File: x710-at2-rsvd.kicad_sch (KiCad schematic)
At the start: 37 parts, among them J8 PinHeader_1x3_P2.54mm_Drill1.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, U9 EZX710AT2_S_LMR5

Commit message: [#86351] Rename project
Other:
- title: 10GbE Expansion -> OCuLink to 10GbE adapter

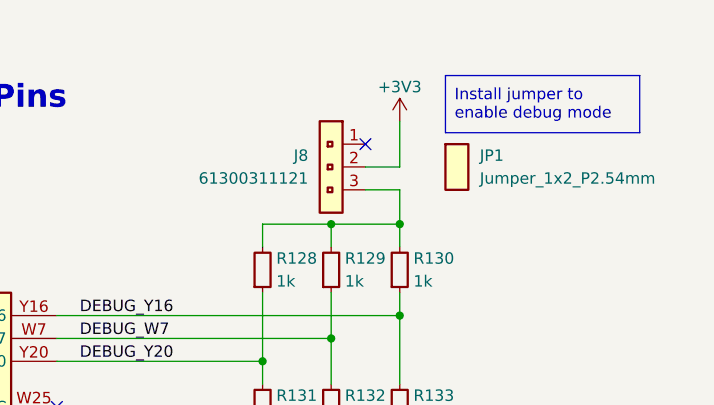
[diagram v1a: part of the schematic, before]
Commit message: [#86617] Change debug EN jumper to a switch
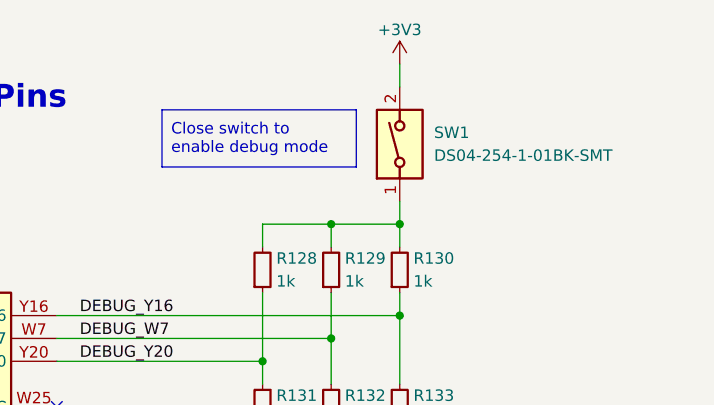
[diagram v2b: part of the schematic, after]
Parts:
- removed J8: PinHeader_1x3_P2.54mm_Drill1.1mm, antmicro-footprints:PinHeader_1x3_P2.54mm_Drill1.1mm, symbol antmicroGenericPinHeaders:PinHeader_1x3_P2.54mm_Drill1.1mm
- removed JP1: Jumper_1x2_P2.54mm, antmicro-footprints:Jumper_1x2_P2.54mm, symbol antmicroShuntsJumpers:Jumper_1x2_P2.54mm
- added SW1: SW_DS04-254-1-01BK-SMT, antmicro-footprints:SW_DS04-254-1-01BK-SMT, symbol antmicroSlideSwitches:SW_DS04-254-1-01BK-SMT
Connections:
- net +3V3: now also SW1.2
- net at R128.2, R129.2, R130.2: now also SW1.1
- no-connect marks 65 -> 64
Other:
- note added: "Close switch to enable debug mode"
- note removed: "Install jumper to enable debug mode"

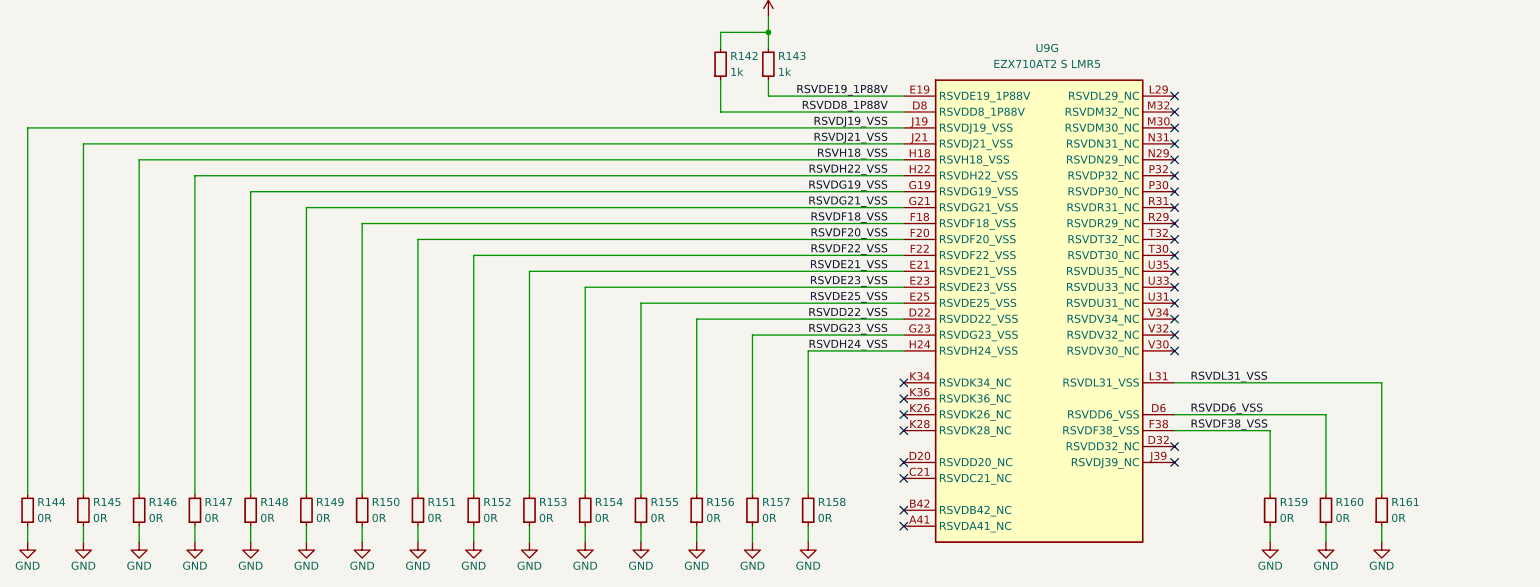
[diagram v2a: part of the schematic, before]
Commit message: [#86351] Replace RSVD_VSS 0Rs with direct connection
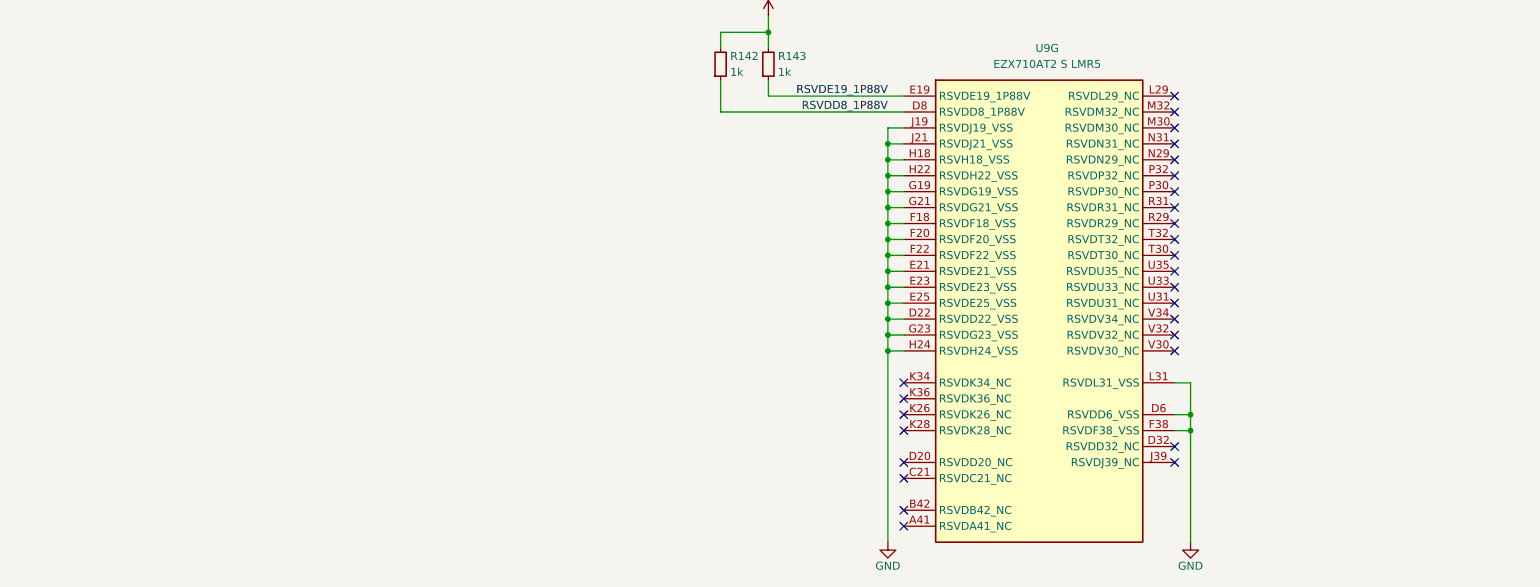
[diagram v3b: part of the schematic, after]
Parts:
- removed R144, R145, R146, R147, R148, R149, R150, R151, R152, R153, R154, R155, R156, R157, R158, R159, R160, R161: R_0R_0402, antmicro-footprints:R_0402_1005Metric, symbol antmicroResistors0402:R_0R_0402
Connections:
- net RSVDD22_VSS is gone; now on net GND: U9.D22 (RSVDD22_VSS)
- net RSVDD6_VSS is gone; now on net GND: U9.D6 (RSVDD6_VSS)
- net RSVDE21_VSS is gone; now on net GND: U9.E21 (RSVDE21_VSS)
- net RSVDE23_VSS is gone; now on net GND: U9.E23 (RSVDE23_VSS)
- net RSVDE25_VSS is gone; now on net GND: U9.E25 (RSVDE25_VSS)
- net RSVDF18_VSS is gone; now on net GND: U9.F18 (RSVDF18_VSS)
- net RSVDF20_VSS is gone; now on net GND: U9.F20 (RSVDF20_VSS)
- net RSVDF22_VSS is gone; now on net GND: U9.F22 (RSVDF22_VSS)
- net RSVDF38_VSS is gone; now on net GND: U9.F38 (RSVDF38_VSS)
- net RSVDG19_VSS is gone; now on net GND: U9.G19 (RSVDG19_VSS)
- net RSVDG21_VSS is gone; now on net GND: U9.G21 (RSVDG21_VSS)
- net RSVDG23_VSS is gone; now on net GND: U9.G23 (RSVDG23_VSS)
- net RSVDH22_VSS is gone; now on net GND: U9.H22 (RSVDH22_VSS)
- net RSVDH24_VSS is gone; now on net GND: U9.H24 (RSVDH24_VSS)
- net RSVDJ19_VSS is gone; now on net GND: U9.J19 (RSVDJ19_VSS)
- net RSVDJ21_VSS is gone; now on net GND: U9.J21 (RSVDJ21_VSS)
- net RSVDL31_VSS is gone; now on net GND: U9.L31 (RSVDL31_VSS)
- net RSVH18_VSS is gone; now on net GND: U9.H18 (RSVH18_VSS)

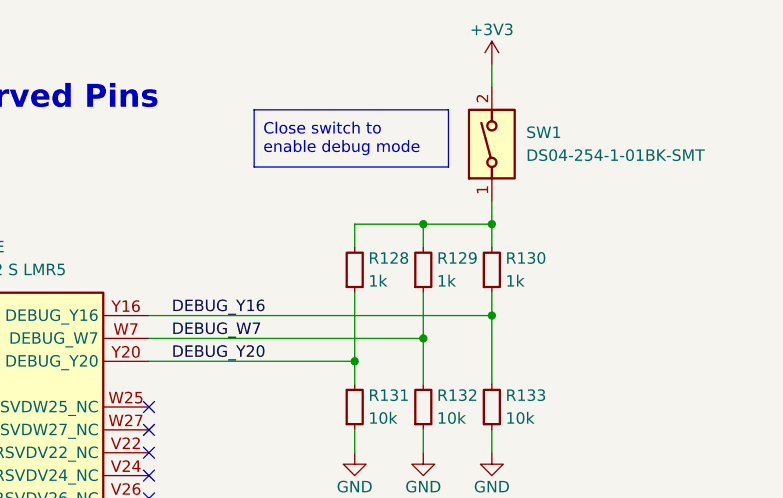
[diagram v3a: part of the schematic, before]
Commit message: [#86351] WIP: Passives component placement
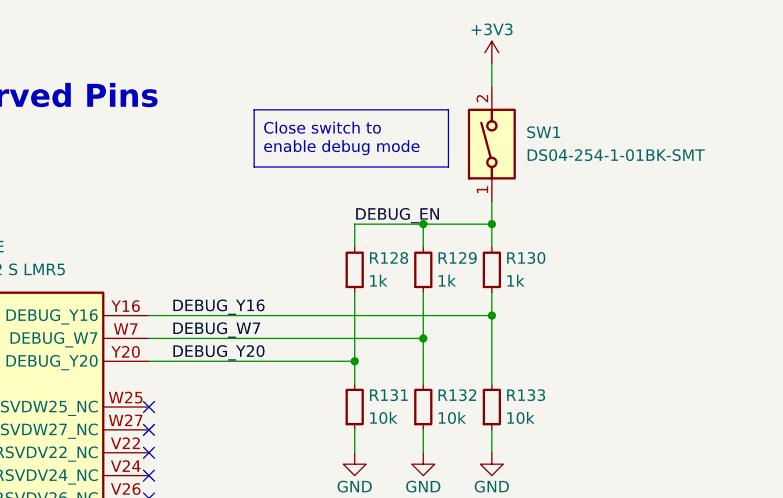
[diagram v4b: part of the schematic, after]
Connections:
- net DEBUG_EN: now reaches R128.2, R129.2, R130.2, SW1.1
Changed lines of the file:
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@@
+		)
+	)
+	(label "DEBUG_EN"
+		(at 261.62 39.37 0)
+		(effects
+			(font
+				(size 1.27 1.27)
+			)
+			(justify left bottom)
 		)
 	)
